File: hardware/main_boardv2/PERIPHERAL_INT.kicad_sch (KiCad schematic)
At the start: 15 parts, among them IC401 PI4IOE5V9537UEX, J401 1x8 Male Pins, J402 2x5 Socket Pins, Q401 NX3020NAK-QR, Q402 NX3020NAK-QR, Q403 NX3020NAK-QR, Q404 NX3020NAK-QR

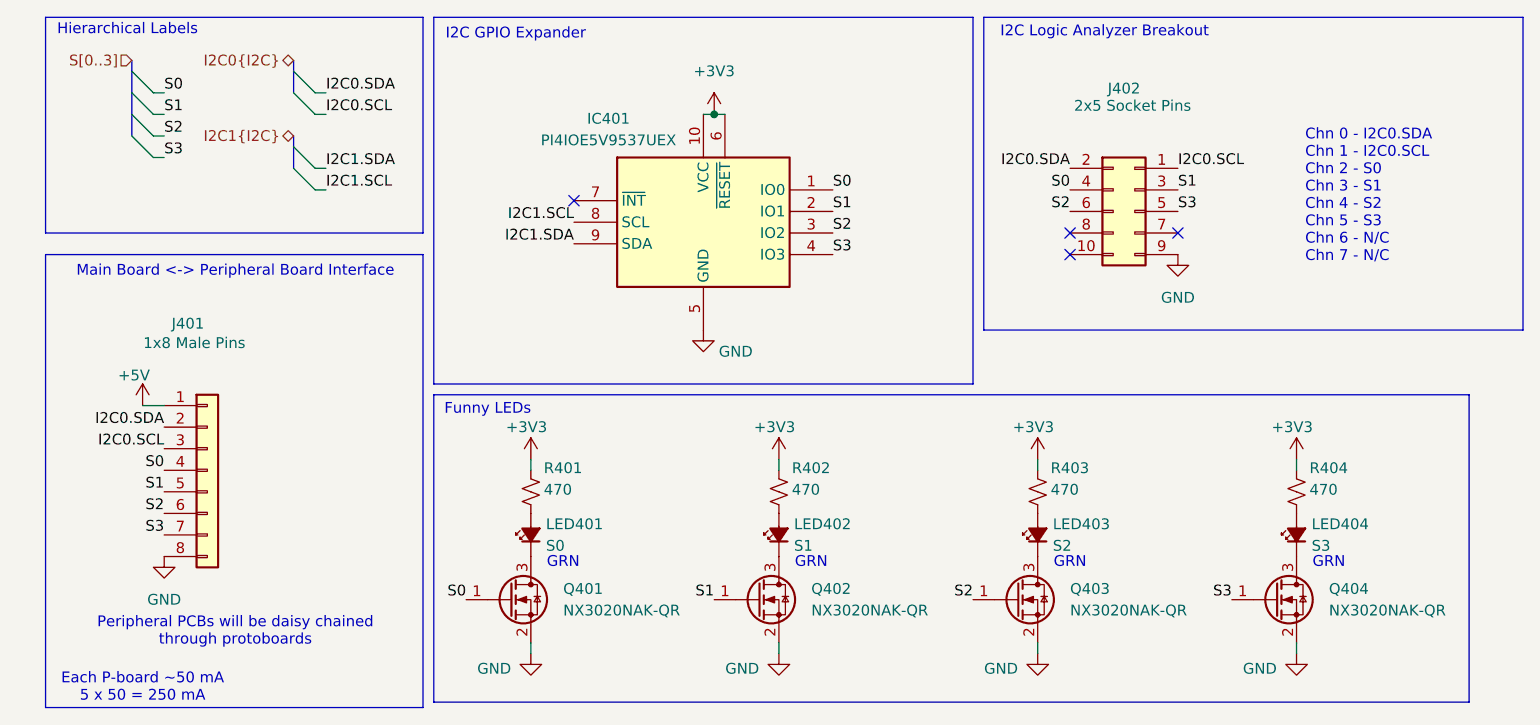
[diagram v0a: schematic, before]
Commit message: dubious hardware schematic 'done'. need to go back and revise passives and verify IC connections, esp the DAC. modified readme
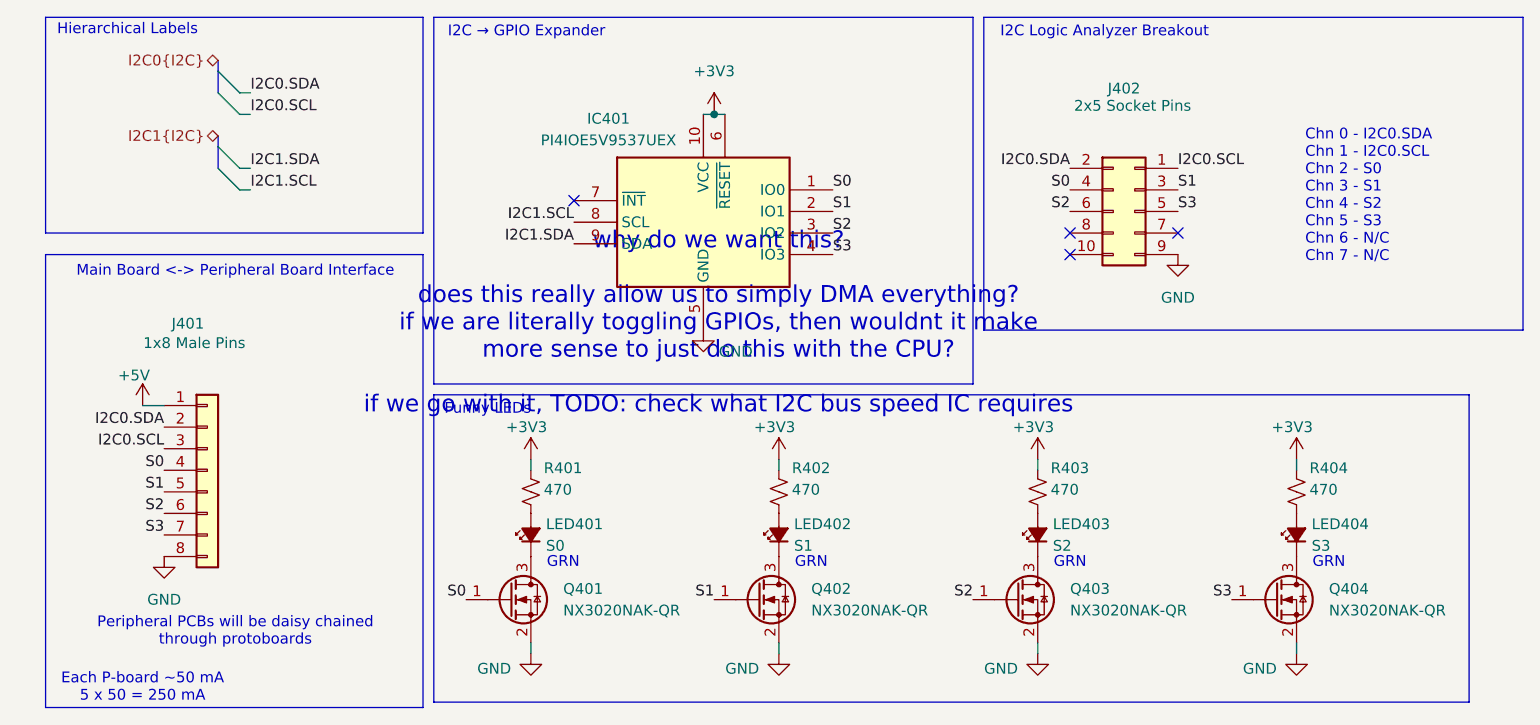
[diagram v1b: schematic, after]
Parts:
- IC401: footprint SOP50P490X110-10N -> SamacSys_Parts:SOP50P490X110-10N
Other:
- note added: "I2C → GPIO Expander"
- note added: "why do we want this? does this really allow us to simply DMA everything? if we are literally toggling GPIOs, then wouldnt it make more sense to just do this with the CPU? if we go with it, TODO: check what I2C bus speed IC requires"
- note removed: "I2C GPIO Expander"
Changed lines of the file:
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@@
+		)
+	)
+	(text "why do we want this?\n\ndoes this really allow us to simply DMA everything?\nif we are literally toggling GPIOs, then wouldnt it make\nmore sense to just do this with the CPU?\n\nif we go with it, TODO: check what I2C bus speed IC requires"
+		(exclude_from_sim no)
+		(at 91.948 48.768 0)
+		(effects
+			(font
+				(size 2 2)
+			)
 		)
 	)
@@
 		)
 	)
-	(text "I2C GPIO Expander"
-		(exclude_from_sim no)
-		(at 68.072 14.732 0)
+	(text "I2C → GPIO Expander"
+		(exclude_from_sim no)
+		(at 69.342 14.478 0)
 		(effects
 			(font
@@
 	)
 	(bus_entry
-		(at 22.86 21.59)
+		(at 33.02 30.48)
 		(size 2.54 2.54)
 		(stroke
@@
 	)
 	(bus_entry
-		(at 41.91 30.48)
+		(at 33.02 19.05)
 		(size 2.54 2.54)
 		(stroke
@@
 	)
 	(bus_entry
-		(at 41.91 19.05)
+		(at 33.02 27.94)
 		(size 2.54 2.54)
 		(stroke
@@
 	)
 	(bus_entry
-		(at 22.86 19.05)
+		(at 33.02 21.59)
 		(size 2.54 2.54)
 		(stroke
@@
 		)
 	)
-	(bus_entry
-		(at 22.86 26.67)
-		(size 2.54 2.54)
-		(stroke
-			(width 0)
-			(type default)
-		)
-	)
-	(bus_entry
-		(at 22.86 24.13)
-		(size 2.54 2.54)
-		(stroke
-			(width 0)
-			(type default)
-		)
-	)
-	(bus_entry
-		(at 41.91 27.94)
-		(size 2.54 2.54)
-		(stroke
-			(width 0)
-			(type default)
-		)
-	)
-	(bus_entry
-		(at 41.91 21.59)
-		(size 2.54 2.54)
-		(stroke
-			(width 0)
-			(type default)
-		)
-	)
 	(wire
 		(pts
@@
 		)
 	)
-	(wire
-		(pts
-			(xy 25.4 29.21) (xy 26.67 29.21)
-		)
-		(stroke
-			(width 0)
-			(type default)
-		)
-	)
 	(bus
 		(pts
-			(xy 41.91 26.67) (xy 41.91 27.94)
+			(xy 33.02 26.67) (xy 33.02 27.94)
 		)
 		(stroke
@@
 		)
 	)
+	(wire
+		(pts
+			(xy 160.02 64.77) (xy 160.02 66.04)
+		)
+		(stroke
+			(width 0)
+			(type default)
+		)
+	)
 	(bus
 		(pts
-			(xy 22.86 17.78) (xy 22.86 19.05)
-		)
-		(stroke
-			(width 0)
-			(type default)
-		)
-	)
-	(wire
-		(pts
-			(xy 160.02 64.77) (xy 160.02 66.04)
-		)
-		(stroke
-			(width 0)
-			(type default)
-		)
-	)
-	(wire
-		(pts
-			(xy 25.4 21.59) (xy 26.67 21.59)
+			(xy 33.02 17.78) (xy 33.02 19.05)
+		)
+		(stroke
+			(width 0)
+			(type default)
+		)
+	)
+	(wire
+		(pts
+			(xy 99.06 87.63) (xy 99.06 86.36)
+		)
+		(stroke
+			(width 0)
+			(type default)
+		)
+	)
+	(wire
+		(pts
+			(xy 35.56 33.02) (xy 36.83 33.02)
+		)
+		(stroke
+			(width 0)
+			(type default)
+		)
+	)
+	(wire
+		(pts
+			(xy 35.56 30.48) (xy 36.83 30.48)
+		)
+		(stroke
+			(width 0)
+			(type default)
+		)
+	)
+	(wire
+		(pts
+			(xy 91.44 24.13) (xy 92.71 24.13)
 		)
 		(stroke
@@
 	(bus
 		(pts
-			(xy 41.91 17.78) (xy 41.91 19.05)
-		)
-		(stroke
-			(width 0)
-			(type default)
-		)
-	)
-	(wire
-		(pts
-			(xy 99.06 87.63) (xy 99.06 86.36)
+			(xy 33.02 19.05) (xy 33.02 21.59)
+		)
+		(stroke
+			(width 0)
+			(type default)
+		)
+	)
+	(wire
+		(pts
+			(xy 129.54 87.63) (xy 129.54 86.36)
+		)
+		(stroke
+			(width 0)
+			(type default)
+		)
+	)
+	(wire
+		(pts
+			(xy 99.06 64.77) (xy 99.06 66.04)
 		)
 		(stroke
@@
 	(bus
 		(pts
-			(xy 22.86 19.05) (xy 22.86 21.59)
-		)
-		(stroke
-			(width 0)
-			(type default)
-		)
-	)
-	(wire
-		(pts
-			(xy 44.45 33.02) (xy 45.72 33.02)
-		)
-		(stroke
-			(width 0)
-			(type default)
-		)
-	)
-	(wire
-		(pts
-			(xy 25.4 26.67) (xy 26.67 26.67)
-		)
-		(stroke
-			(width 0)
-			(type default)
-		)
-	)
-	(wire
-		(pts
-			(xy 44.45 30.48) (xy 45.72 30.48)
-		)
-		(stroke
-			(width 0)
-			(type default)
-		)
-	)
-	(bus
-		(pts
-			(xy 22.86 24.13) (xy 22.86 26.67)
-		)
-		(stroke
-			(width 0)
-			(type default)
-		)
-	)
-	(wire
-		(pts
-			(xy 91.44 24.13) (xy 92.71 24.13)
-		)
-		(stroke
-			(width 0)
-			(type default)
-		)
-	)
-	(bus
-		(pts
-			(xy 41.91 19.05) (xy 41.91 21.59)
-		)
-		(stroke
-			(width 0)
-			(type default)
-		)
-	)
-	(wire
-		(pts
-			(xy 25.4 24.13) (xy 26.67 24.13)
-		)
-		(stroke
-			(width 0)
-			(type default)
-		)
-	)
-	(bus
-		(pts
-			(xy 22.86 21.59) (xy 22.86 24.13)
-		)
-		(stroke
-			(width 0)
-			(type default)
-		)
-	)
-	(wire
-		(pts
-			(xy 129.54 87.63) (xy 129.54 86.36)
-		)
-		(stroke
-			(width 0)
-			(type default)
-		)
-	)
-	(wire
-		(pts
-			(xy 99.06 64.77) (xy 99.06 66.04)
-		)
-		(stroke
-			(width 0)
-			(type default)
-		)
-	)
-	(bus
-		(pts
-			(xy 41.91 27.94) (xy 41.91 30.48)
+			(xy 33.02 27.94) (xy 33.02 30.48)
 		)
 		(stroke
@@
 	(wire
 		(pts
-			(xy 44.45 24.13) (xy 45.72 24.13)
-		)
-		(stroke
-			(width 0)
-			(type default)
-		)
-	)
-	(wire
-		(pts
-			(xy 44.45 21.59) (xy 45.72 21.59)
+			(xy 35.56 24.13) (xy 36.83 24.13)
+		)
+		(stroke
+			(width 0)
+			(type default)
+		)
+	)
+	(wire
+		(pts
+			(xy 35.56 21.59) (xy 36.83 21.59)
 		)
 		(stroke
@@
 	)
 	(label "I2C1.SDA"
-		(at 45.72 30.48 0)
+		(at 36.83 30.48 0)
 		(effects
 			(font
@@
 		)
 	)
-	(label "S3"
-		(at 26.67 29.21 0)
-		(effects
-			(font
-				(size 1.27 1.27)
-			)
-			(justify left bottom)
-		)
-	)
 	(label "I2C0.SDA"
-		(at 45.72 21.59 0)
+		(at 36.83 21.59 0)
 		(effects
 			(font
@@
 		)
 	)
-	(label "S0"
-		(at 26.67 21.59 0)
-		(effects
-			(font
-				(size 1.27 1.27)
-			)
-			(justify left bottom)
-		)
-	)
 	(label "S1"
 		(at 91.44 81.28 180)
@@
 		)
 	)
-	(label "S1"
-		(at 26.67 24.13 0)
-		(effects
-			(font
-				(size 1.27 1.27)
-			)
-			(justify left bottom)
-		)
-	)
 	(label "S3"
 		(at 26.67 73.66 180)
@@
 		)
 	)
-	(label "S2"
-		(at 26.67 26.67 0)
-		(effects
-			(font
-				(size 1.27 1.27)
-			)
-			(justify left bottom)
-		)
-	)
 	(label "S1"
 		(at 146.05 33.02 0)
@@
 	)
 	(label "I2C0.SCL"
-		(at 45.72 24.13 0)
+		(at 36.83 24.13 0)
 		(effects
 			(font
@@
 	)
 	(label "I2C1.SCL"
-		(at 45.72 33.02 0)
+		(at 36.83 33.02 0)
 		(effects
 			(font
@@
 	(hierarchical_label "I2C1{I2C}"
 		(shape bidirectional)
-		(at 41.91 26.67 180)
+		(at 33.02 26.67 180)
 		(effects
 			(font
@@
 	(hierarchical_label "I2C0{I2C}"
 		(shape bidirectional)
-		(at 41.91 17.78 180)
-		(effects
-			(font
-				(size 1.27 1.27)
-			)
-			(justify right)
-		)
-	)
-	(hierarchical_label "S[0..3]"
-		(shape input)
-		(at 22.86 17.78 180)
+		(at 33.02 17.78 180)
 		(effects
 			(font
@@
 			)
 		)
-		(property "Footprint" "SOP50P490X110-10N"
+		(property "Footprint" "SamacSys_Parts:SOP50P490X110-10N"
 			(at 101.6 126.67 0)
 			(effects

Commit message: schematic sorta done? resized all RC packages to 0805
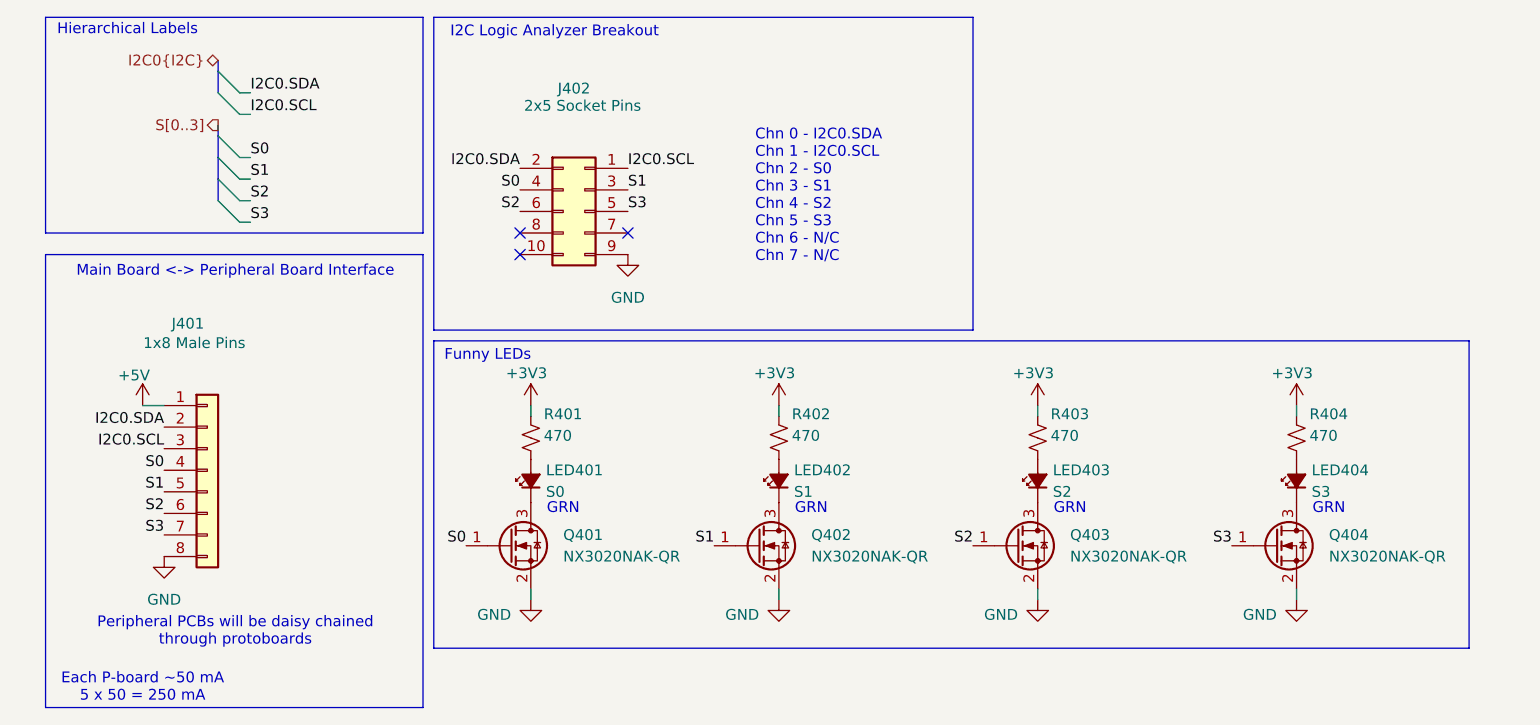
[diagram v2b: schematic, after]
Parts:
- removed IC401: PI4IOE5V9537UEX, SamacSys_Parts:SOP50P490X110-10N, symbol SamacSys_Parts:PI4IOE5V9537UEX
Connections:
- no-connect marks 4 -> 3
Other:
- note removed: "I2C → GPIO Expander"
- note removed: "why do we want this? does this really allow us to simply DMA everything? if we are literally toggling GPIOs, then wouldnt it make more sense to just do this with the CPU? if we go with it, TODO: check what I2C bus speed IC requires"
- moved on the sheet: J402, LED401, LED402, LED403, LED404, Q401, Q402, Q403, Q404, R401, R402, R403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

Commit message: resized all package to 0603
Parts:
- R401, R402, R403, R404: footprint Resistor_SMD:R_0805_2012Metric -> Resistor_SMD:R_0603_1608Metric
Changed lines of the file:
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@@
 			)
 		)
-		(property "Footprint" "Resistor_SMD:R_0805_2012Metric"
+		(property "Footprint" "Resistor_SMD:R_0603_1608Metric"
 			(at 71.628 62.23 90)
 			(effects
@@
 			)
 		)
-		(property "Footprint" "Resistor_SMD:R_0805_2012Metric"
+		(property "Footprint" "Resistor_SMD:R_0603_1608Metric"
 			(at 161.798 62.23 90)
 			(effects
@@
 			)
 		)
-		(property "Footprint" "Resistor_SMD:R_0805_2012Metric"
+		(property "Footprint" "Resistor_SMD:R_0603_1608Metric"
 			(at 131.318 62.23 90)
 			(effects
@@
 			)
 		)
-		(property "Footprint" "Resistor_SMD:R_0805_2012Metric"
+		(property "Footprint" "Resistor_SMD:R_0603_1608Metric"
 			(at 100.838 62.23 90)
 			(effects
